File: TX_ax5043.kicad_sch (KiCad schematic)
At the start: 27 parts, among them P6 CONUFL001-SMD-T, P7 CONUFL001-SMD-T, Q7 DMP2037U-7, U23 AX5043

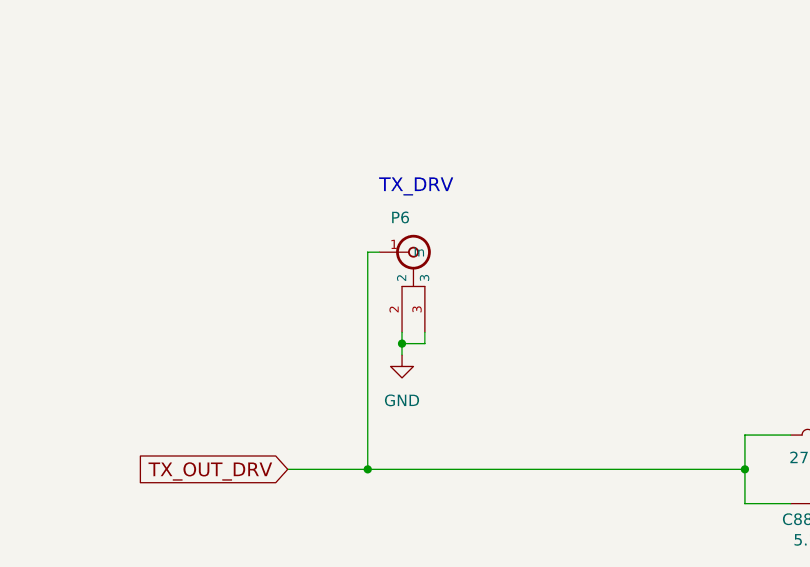
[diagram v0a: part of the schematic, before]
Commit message: Clean up the U.FL connectors a little more
Re-add the ones for TX/RX so both MMCX and U.FL are available.

Move P8 to a better location.

Signed-off-by: Corey Minyard <corey@minyard.net>
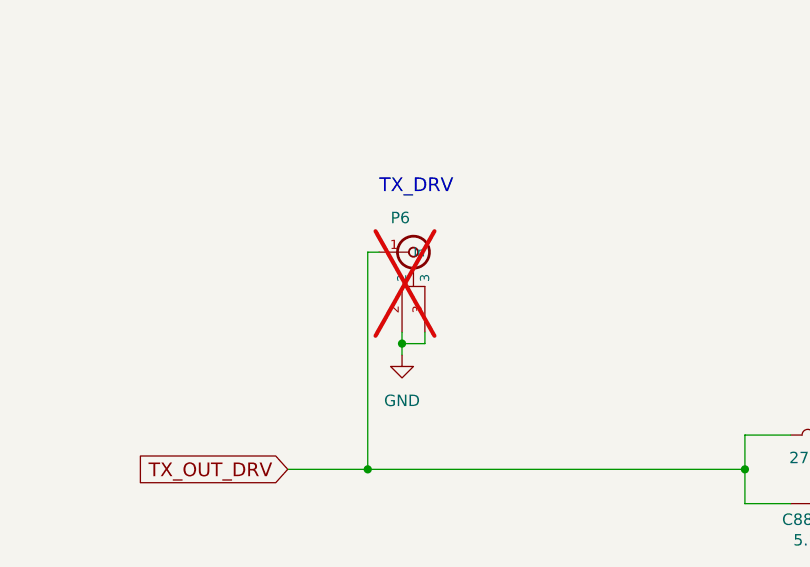
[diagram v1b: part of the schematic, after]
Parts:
- P6: now not fitted; now left out of the parts list
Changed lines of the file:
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@@
 		(unit 1)
 		(exclude_from_sim no)
-		(in_bom yes)
+		(in_bom no)
 		(on_board yes)
-		(dnp no)
+		(dnp yes)
 		(property "Reference" "P6"
 			(at 124.46 107.95 0)

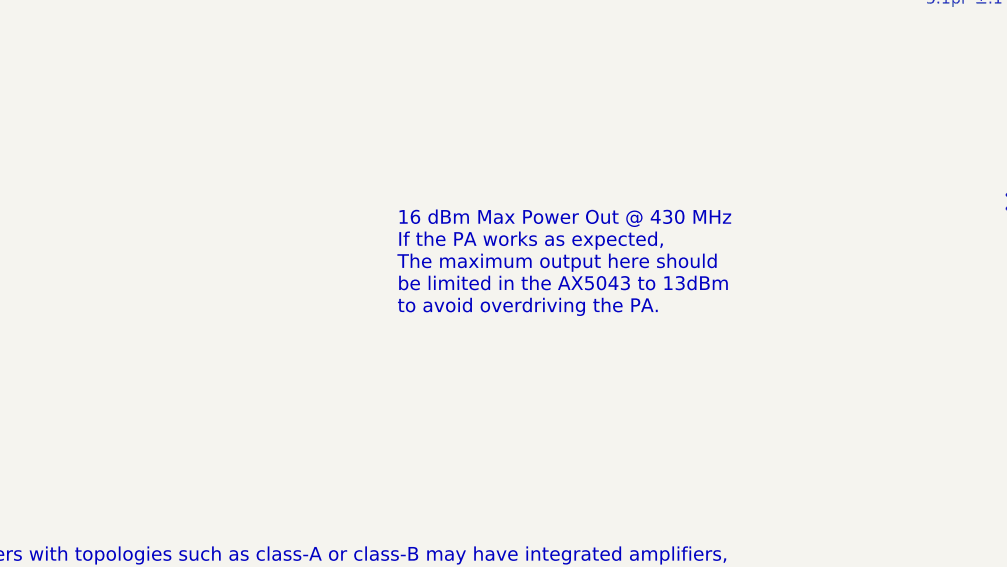
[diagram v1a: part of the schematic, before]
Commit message: Rework PA input some more
Signed-off-by: Corey Minyard <corey@minyard.net>
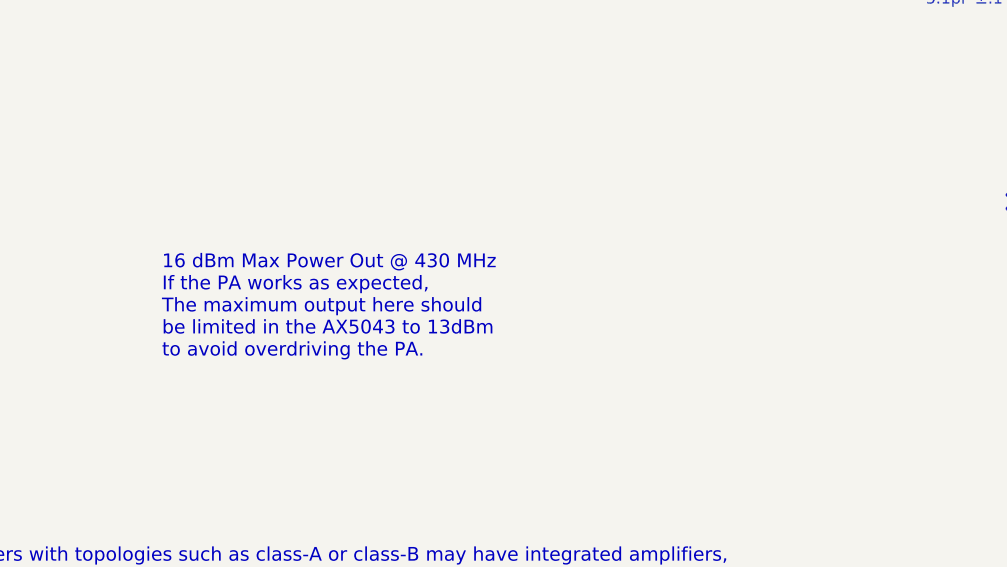
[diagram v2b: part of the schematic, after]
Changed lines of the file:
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@@
 	(text "16 dBm Max Power Out @ 430 MHz\nIf the PA works as expected,\nThe maximum output here should\nbe limited in the AX5043 to 13dBm\nto avoid overdriving the PA."
 		(exclude_from_sim no)
-		(at 110.49 179.07 0)
+		(at 84.328 183.896 0)
 		(effects
 			(font

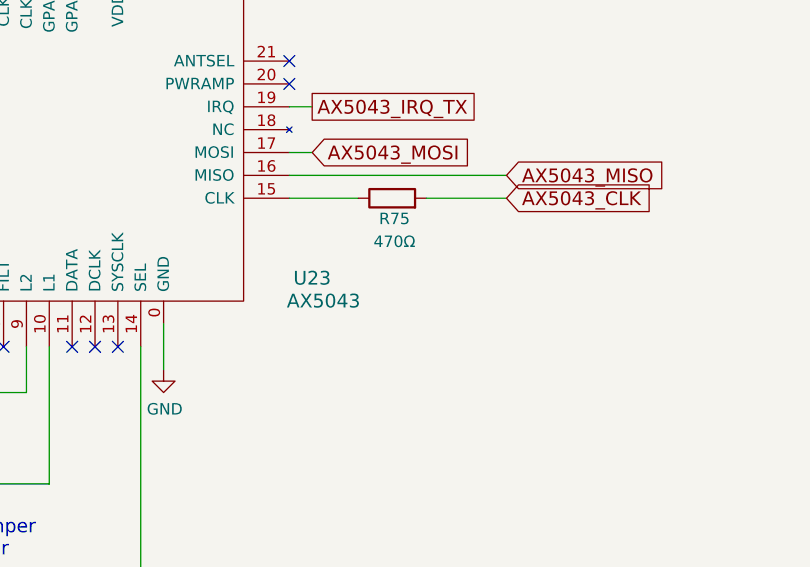
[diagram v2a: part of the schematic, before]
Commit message: Add a DAC to the PA Iref input
Allow the power the PA uses to be directly controlled.

Signed-off-by: Corey Minyard <corey@minyard.net>
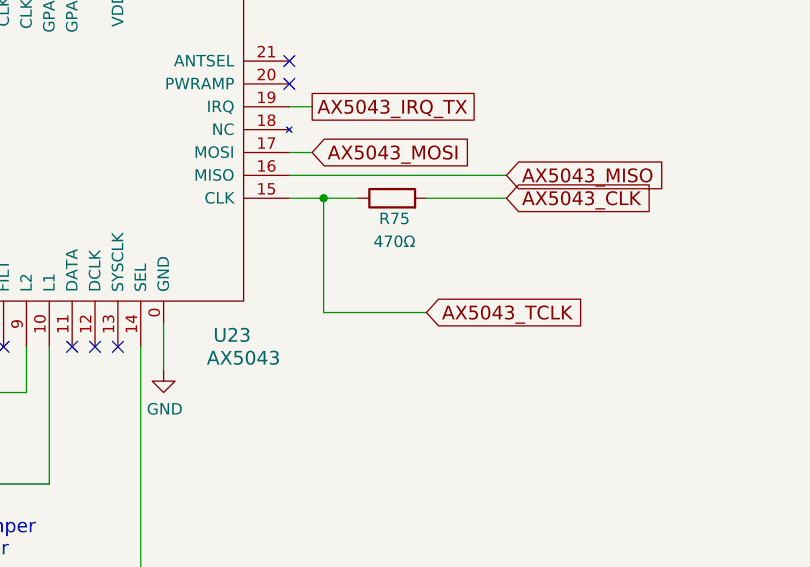
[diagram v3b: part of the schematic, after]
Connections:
- net AX5043_TCLK: now reaches R75.1, U23.15 (CLK)
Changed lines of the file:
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@@
 	)
 	(junction
+		(at 293.37 144.78)
+		(diameter 0)
+		(color 0 0 0 0)
+	)
+	(junction
 		(at 289.56 100.33)
 		(diameter 0)
@@
 	(wire
 		(pts
+			(xy 304.8 157.48) (xy 293.37 157.48)
+		)
+		(stroke
+			(width 0)
+			(type default)
+		)
+	)
+	(wire
+		(pts
 			(xy 176.53 139.7) (xy 184.15 139.7)
 		)
@@
 	(wire
 		(pts
+			(xy 293.37 144.78) (xy 297.18 144.78)
+		)
+		(stroke
+			(width 0)
+			(type default)
+		)
+	)
+	(wire
+		(pts
 			(xy 242.57 166.37) (xy 242.57 176.53)
 		)
@@
 	(wire
 		(pts
+			(xy 293.37 157.48) (xy 293.37 144.78)
+		)
+		(stroke
+			(width 0)
+			(type default)
+		)
+	)
+	(wire
+		(pts
 			(xy 242.57 176.53) (xy 248.92 176.53)
 		)
@@
 	(wire
 		(pts
-			(xy 289.56 144.78) (xy 297.18 144.78)
+			(xy 289.56 144.78) (xy 293.37 144.78)
 		)
 		(stroke
@@
 		)
 	)
+	(global_label "AX5043_TCLK"
+		(shape input)
+		(at 304.8 157.48 0)
+		(fields_autoplaced yes)
+		(effects
+			(font
+				(size 1.524 1.524)
+			)
+			(justify left)
+		)
+		(property "Intersheetrefs" "${INTERSHEET_REFS}"
+			(at 322.764 157.48 0)
+			(effects
+				(font
+					(size 1.27 1.27)
+				)
+				(justify left)
+				(hide yes)
+			)
+		)
+	)
 	(global_label "Clock_TX"
 		(shape input)
@@
 		(dnp no)
 		(property "Reference" "U23"
-			(at 292.1 153.67 0)
+			(at 283.21 160.02 0)
 			(effects
 				(font
@@
 		)
 		(property "Value" "AX5043"
-			(at 293.37 156.21 0)
+			(at 284.48 162.56 0)
 			(effects
 				(font

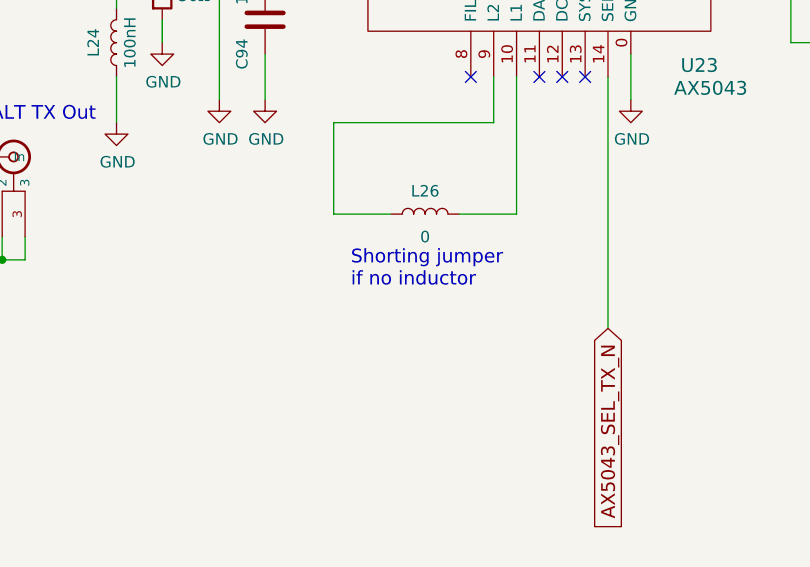
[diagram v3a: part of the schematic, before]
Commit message: Change the AX5043 TX PLL inductor to 18nH
It works fine at 435MHz and 145MHz.

Add notes on using this for loopback testing.

Signed-off-by: Corey Minyard <corey@minyard.net>
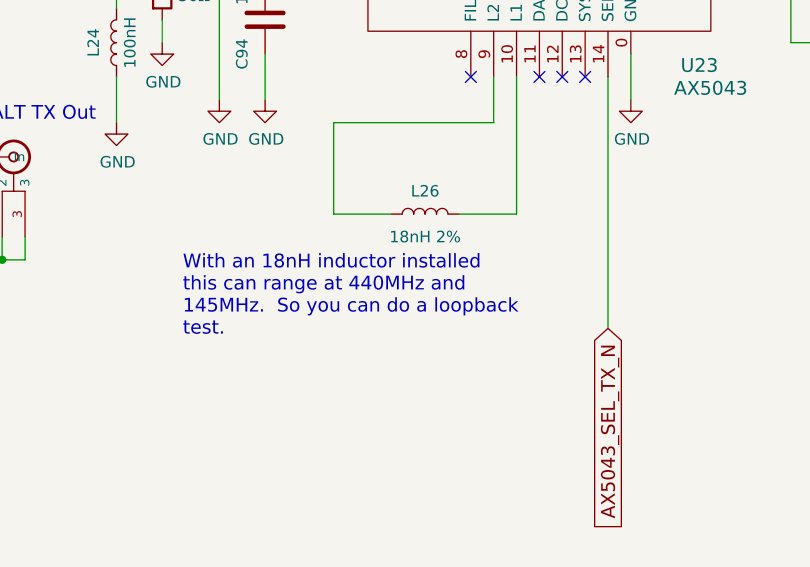
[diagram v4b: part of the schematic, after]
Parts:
- L26: value 0 -> 18nH 2%
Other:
- note added: "With an 18nH inductor installed this can range at 440MHz and 145MHz. So you can do a loopback test."
- note removed: "Shorting jumper if no inductor"
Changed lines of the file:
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@@
 		)
 	)
-	(text "Shorting jumper\nif no inductor"
+	(text "With an 18nH inductor installed\nthis can range at 440MHz and\n145MHz.  So you can do a loopback\ntest."
 		(exclude_from_sim no)
-		(at 244.475 184.785 0)
+		(at 225.806 190.246 0)
 		(effects
 			(font
@@
 	)
 	(symbol
-		(lib_id "Device:L")
-		(at 252.73 176.53 90)
-		(unit 1)
-		(exclude_from_sim no)
-		(in_bom yes)
-		(on_board yes)
-		(dnp no)
-		(property "Reference" "L26"
-			(at 252.73 173.99 90)
-			(effects
-				(font
-					(size 1.27 1.27)
-				)
-			)
-		)
-		(property "Value" "0"
-			(at 252.73 179.07 90)
-			(effects
-				(font
-					(size 1.27 1.27)
-				)
-			)
-		)
-		(property "Footprint" "Inductor_SMD:L_0603_1608Metric_Pad1.05x0.95mm_HandSolder"
-			(at 252.73 176.53 0)
-			(effects
-				(font
-					(size 1.27 1.27)
-				)
-				(hide yes)
-			)
-		)
-		(property "Datasheet" "~"
-			(at 252.73 176.53 0)
-			(effects
-				(font
-					(size 1.27 1.27)
-				)
-				(hide yes)
-			)
-		)
-		(property "Description" ""
-			(at 252.73 176.53 0)
-			(effects
-				(font
-					(size 1.27 1.27)
-				)
-			)
-		)
-		(pin "1"
-		)
-		(pin "2"
-		)
-		(instances
-			(project "PacSat_Dev_RevD_240614"
-				(path "/cc9f42d2-6985-41ac-acab-5ab7b01c5b38/d9a83ee4-3280-49b9-88b8-54d26cbd8ed1/2fc9a4ba-520e-46cf-be0c-1f13bbb64152"
-					(reference "L26")
-					(unit 1)
-				)
-			)
-		)
-	)
-	(symbol
 		(lib_id "Device:R")
 		(at 300.99 144.78 90)
@@
 					(unit 1)
 				)
+			)
+		)
+	)
+	(symbol
+		(lib_id "Device:L")
+		(at 252.73 176.53 90)
+		(unit 1)
+		(exclude_from_sim no)
+		(in_bom yes)
+		(on_board yes)
+		(dnp no)
+		(property "Reference" "L26"
+			(at 252.73 173.99 90)
+			(effects
+				(font
+					(size 1.27 1.27)
+				)
+			)
+		)
+		(property "Value" "18nH 2%"
+			(at 252.73 179.07 90)
+			(effects
+				(font
+					(size 1.27 1.27)
+				)
+			)
+		)
+		(property "Footprint" "Inductor_SMD:L_0603_1608Metric_Pad1.05x0.95mm_HandSolder"
+			(at 252.73 176.53 0)
+			(effects
+				(font
+					(size 1.27 1.27)
+				)
+				(hide yes)
+			)
+		)
+		(property "Datasheet" "~"
+			(at 252.73 176.53 0)
+			(effects
+				(font
+					(size 1.27 1.27)
+				)
+				(hide yes)
+			)
+		)
+		(property "Description" ""
+			(at 252.73 176.53 0)
+			(effects
+				(font
+					(size 1.27 1.27)
+				)
+			)
+		)
+		(pin "1"
+		)
+		(pin "2"
+		)
+		(instances
+			(project "PacSat_AFSK"
+				(path "/cc9f42d2-6985-41ac-acab-5ab7b01c5b38/d9a83ee4-3280-49b9-88b8-54d26cbd8ed1/2fc9a4ba-520e-46cf-be0c-1f13bbb64152"
+					(reference "L26")
+					(unit 1)
+				)

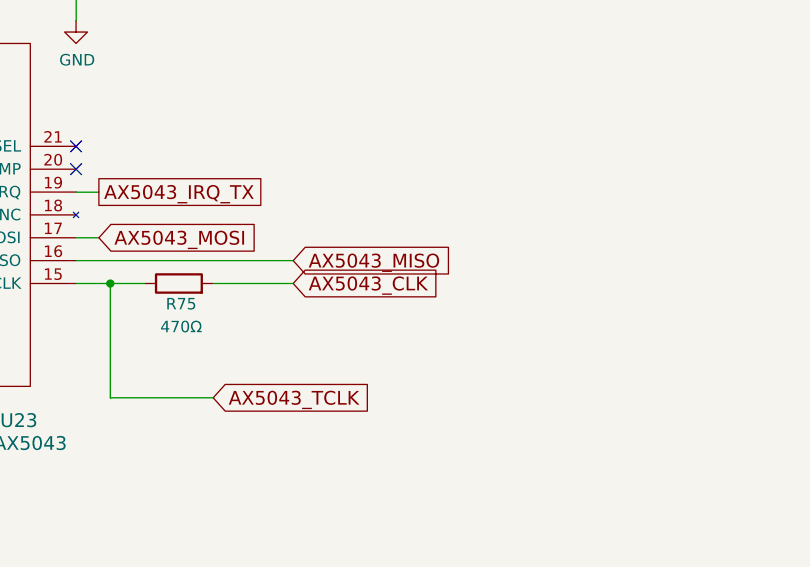
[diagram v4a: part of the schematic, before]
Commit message: Get the board ready for operation
Make the board ready as a final product, remove the lab testing portions
and add in the things required for full operation.

Signed-off-by: Corey Minyard <corey@minyard.net>
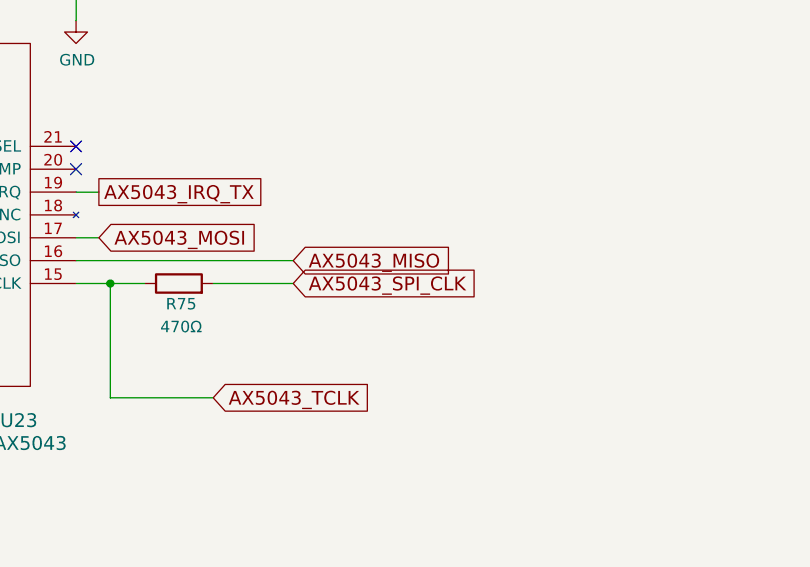
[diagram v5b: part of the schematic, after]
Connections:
- net AX5043_CLK renamed AX5043_SPI_CLK
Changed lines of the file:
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@@
 		)
 	)
-	(global_label "AX5043_CLK"
+	(global_label "AX5043_SPI_CLK"
 		(shape input)
 		(at 313.69 144.78 0)
